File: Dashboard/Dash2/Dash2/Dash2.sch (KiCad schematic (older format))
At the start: 121 parts, among them J101 Left_Signal, J102 Right_Signal, J103 Brake Light, J104 Headlight, J105 Backup, J106 BPS_PWR, J107 SWD, J108 Motor-C, J109 Motor-P, J110 Array-C, J111 Array-P, J112 Conn_01x03_Female, J113 Conn_01x03_Female, J114 JTAG, J115 Gecko_Cable, SW101 CRUISE_SET, SW102 CRUISE, SW103 HAZARD, SW104 HEADLIGHT_SW, SW105 F/R_SW, SW106 BACKUP_SW, SW107 SW_Rotary2x6, SW108 TURN_SIGNAL_SW, SW109 KILL_SW, SW110 RESET, U101 EL3H7, U102 EL3H7, U103 EL3H7, U104 EL3H7, U105 EL3H7, U106 EL3H7, U107 STM32F413ZHTx, U108 EL3H7, U109 EL3H7, U110 EL3H7, U111 EL3H7, Y101 Crystal, Y102 Crystal

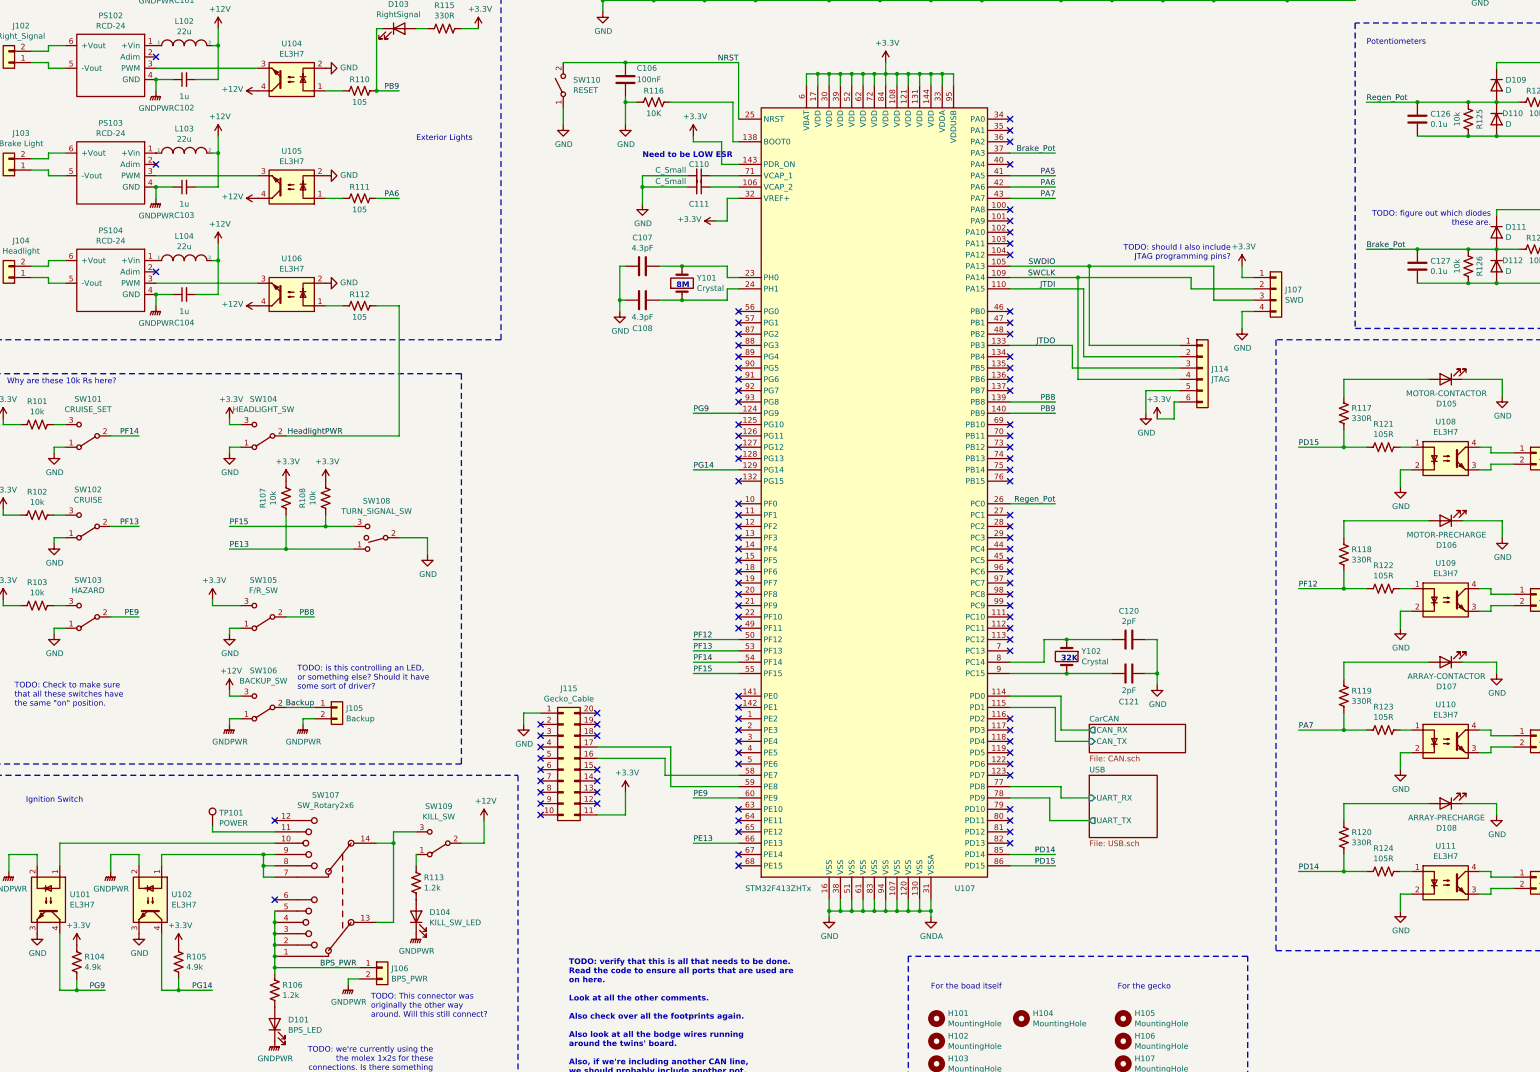
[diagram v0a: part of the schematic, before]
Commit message: Add complete layout of the board
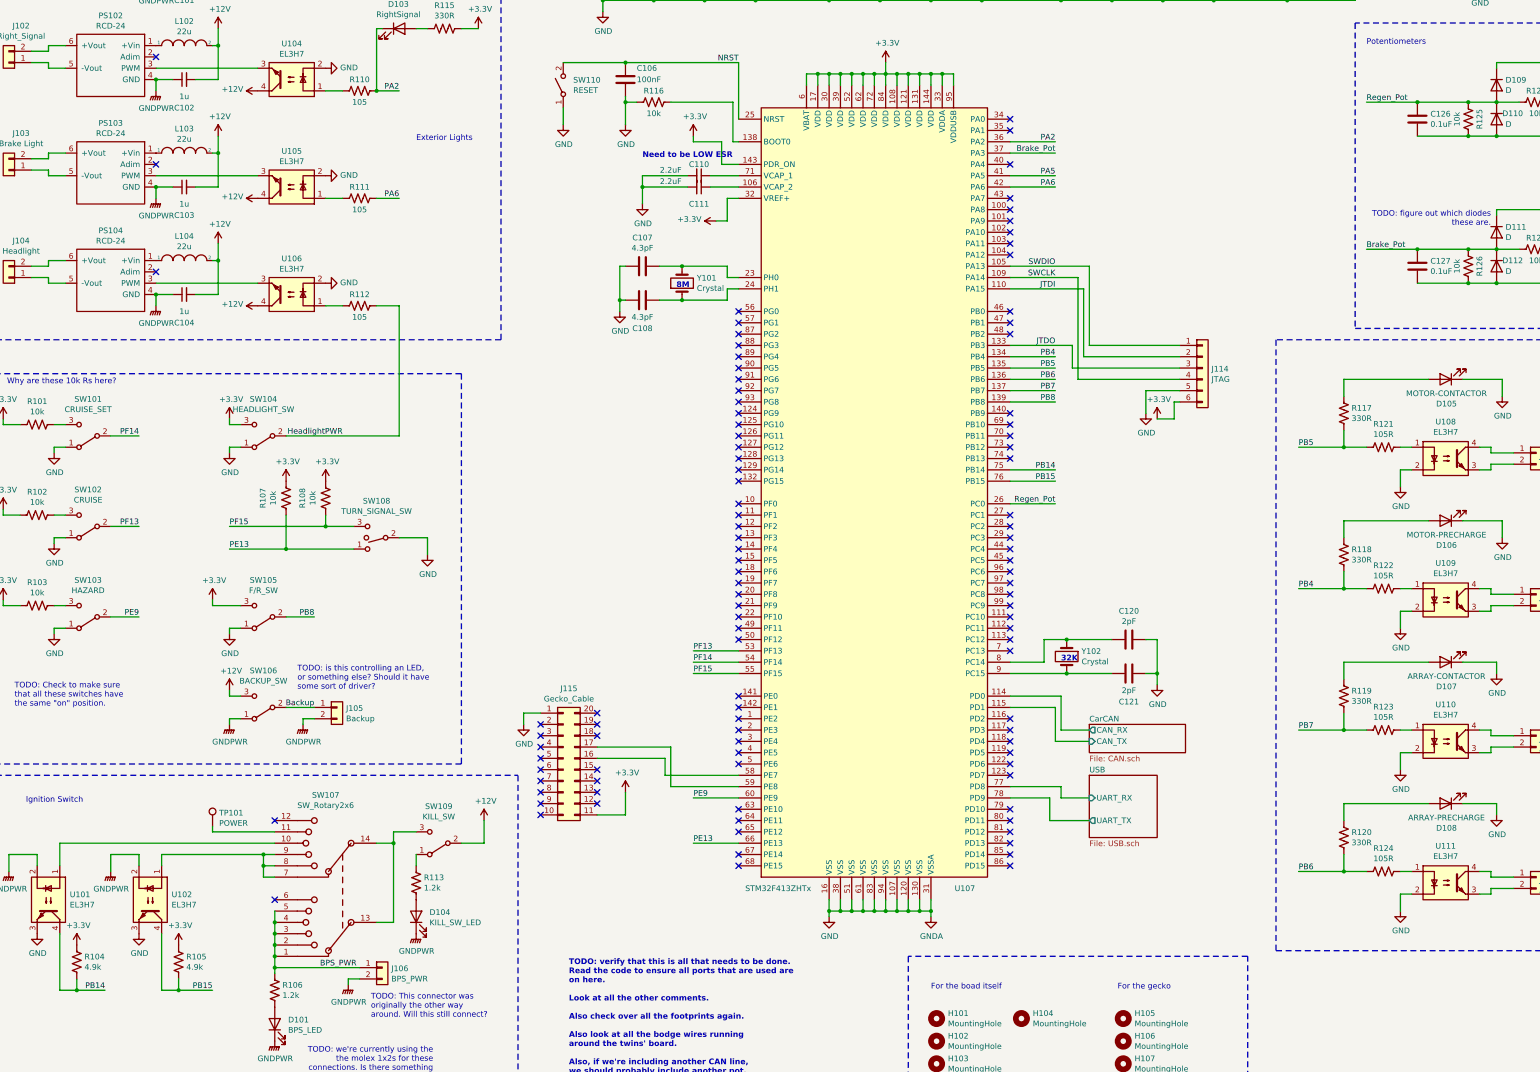
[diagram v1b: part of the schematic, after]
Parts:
- removed J107: SWD, Connector_PinHeader_2.54mm:PinHeader_1x04_P2.54mm_Vertical, symbol Connector_Generic:Conn_01x04
- C101, C102, C103, C104: Mouser Part Number (none) -> 80-C0805C105J3RECAUT
- C105, C106, C109, C112, C113, C114, C115, C116, C117, C118, C119, C122, C123, C125: Mouser Part Number (none) -> 80-C0805C104K3R
- C107, C108: Mouser Part Number (none) -> 80-C0805C479K1G
- C110, C111: value C_Small -> 2.2uF; Mouser Part Number (none) -> 80-C0805C225M4RECLR
- C120, C121: Mouser Part Number (none) -> 80-C0805C209C5G
- C124: Mouser Part Number (none) -> 80-C0805C475K3RAUTO
- C126, C127: value 0.1u -> 0.1uF; Mouser Part Number (none) -> 80-C0805C104K3R
- D109, D110, D111, D112: Mouser Part Number (none) -> 581-SD0805S020S1R0
- J115: Mouser Part Number (none) -> 517-N2520-5002RB
- L101, L102, L103, L104: footprint Diode_SMD:D_0805_2012Metric -> Inductor_SMD:L_0805_2012Metric; Mouser Part Number (none) -> 81-LQM21DH220M70L
- PS101, PS102, PS103, PS104: Mouser Part Number (none) -> 919-RCD-24-0.35
- R101, R102, R103, R107, R108, R125, R126, R127, R128: Mouser Part Number (none) -> 71-CRCW080510K0FKEAC
- R104, R105: Mouser Part Number (none) -> 71-CRCW08054K99FKEAC
- R106, R113: Mouser Part Number (none) -> 71-CRCW08051K20FKEA
- R109, R110, R111, R112, R121, R122, R123, R124: Mouser Part Number (none) -> 71-CRCW0805105RFKEA
- R114, R115, R117, R118, R119, R120: Mouser Part Number (none) -> 71-CRCW0805330RFKEAC
- R116: value 10K -> 10k; Mouser Part Number (none) -> 71-CRCW080510K0FKEAC
- SW107: Mouser Part Number (none) -> 10WA325
- SW110: Mouser Part Number (none) -> 653-B3SL-1002P
- U101, U102, U103, U104, U105, U106, U108, U109, U110, U111: Mouser Part Number (none) -> 638-EL3H7DTAVG
- Y102: footprint Crystal:Crystal_SMD_TXC_7A-2Pin_5x3.2mm -> Crystal:Crystal_SMD_TXC_9HT11-2Pin_2.0x1.2mm
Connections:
- net PB4: now reaches U107.134 (PB4)
- net PB4: now also R118.2, R122.2
- net PB5: now reaches U107.135 (PB5)
- net PB5: now also R117.2, R121.2
- net PB6: now reaches U107.136 (PB6)
- net PB6: now also R120.2, R124.2
- net PB7: now reaches U107.137 (PB7)
- net PB7: now also R119.2, R123.2
- net PA2: now reaches U107.36 (PA2)
- net PA2: now also D103.1 (K), R110.2
- net PB14: now reaches U107.75 (PB14)
- net PB14: now also R104.2, U101.4
- net PB15: now reaches U107.76 (PB15)
- net PB15: now also R105.2, U102.4
- removed net PA7: R119.2, R123.2, U107.43 (PA7)
- removed net PB9: D103.1 (K), R110.2, U107.140 (PB9)
- removed net PD14: R120.2, R124.2, U107.85 (PD14)
- removed net PD15: R117.2, R121.2, U107.86 (PD15)
- removed net PF12: R118.2, R122.2, U107.50 (PF12)
- removed net PG14: R105.2, U102.4, U107.129 (PG14)
- removed net PG9: R104.2, U101.4, U107.124 (PG9)
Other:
- note removed: "TODO: should I also include\nJTAG programming pins?"

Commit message: Add LED board and timing circuitry. The LED board is not yet integrated with the Dash.
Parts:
- added Q? (x4): Q_PNP_BCE, symbol Device:Q_PNP_BCE
- added R? (x3): 100k, symbol Device:R_Small_US
- renumbered J115 to J107, J114 to J108, J108 to J109, J109 to J110, J110 to J111, J111 to J112, J112 to J113, J113 to J114
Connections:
- net HeadlightPWR: now also U107.67 (PE14)
- net MotorCAN/CAN_RX: now reaches U107.73 (PB12)
- net MotorCAN/CAN_TX: now reaches U107.74 (PB13)
- net PA2: no longer names the net of D103.1 (K), R110.2
- net PA2: now also Q?.3 (E), Q?.3 (E); no longer U107.36 (PA2)
- net PA5: no longer names the net of D102.1 (K), R109.2
- net PA5: now also Q?.3 (E), Q?.3 (E); no longer U107.41 (PA5)
- net PA6 renamed BK_LGHT
- net PB14 renamed IG1
- net PB15 renamed IG2
- net PB4 renamed M_PRCHG
- net PB5 renamed M_CNCTR
- net PB6 renamed A_PRCHG
- net PB7 renamed A_CNCTR
- net PB8 renamed FR_SW
- net PE13 renamed RIGHT_SW
- net RIGHT_SW: now also R?.1
- net PE9 renamed HZD_SW
- net HZD_SW: now also R?.1
- net PF13 renamed CRUZ_EN
- net PF14 renamed CRUZ_ST
- net PF15 renamed LEFT_SW
- net LEFT_SW: now also R?.1
- new net: Q?.1 (B), R?.2 (x2)
- new net: Q?.1 (B), Q?.1 (B), R?.2
- new net lights-timer/BLINK: Q?.2 (C), Q?.2 (C), Q?.2 (C), Q?.2 (C)
- no-connect marks 105 -> 104
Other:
- note added: "These are negative-logic signals."
- note added: "Timing control for the lights"
- moved on the sheet: C101, C102, C103, C104, C105, C106, C107, C108, C109, C110, C111, C112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
